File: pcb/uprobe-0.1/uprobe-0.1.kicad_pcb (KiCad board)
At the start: 2 copper layers, 33.5 x 77 mm, 5 parts, among them J1 uConsoleEXT

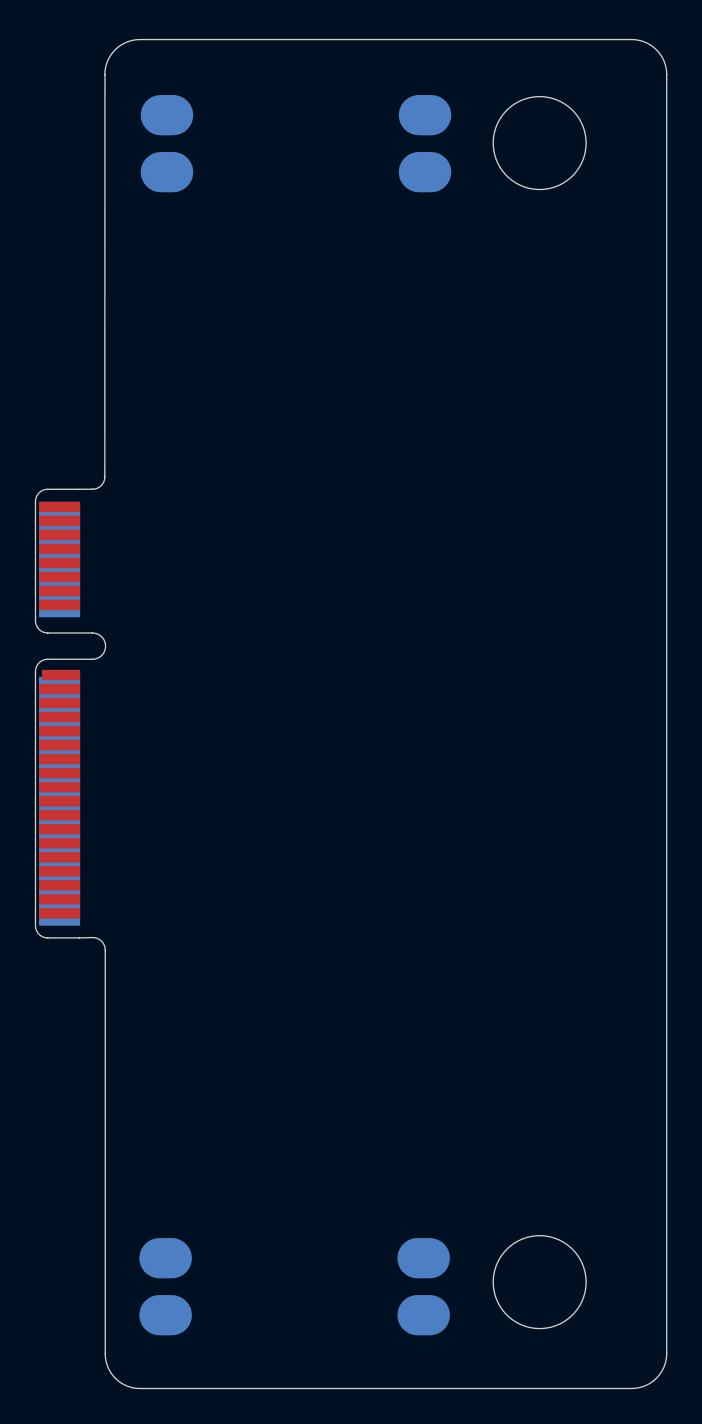
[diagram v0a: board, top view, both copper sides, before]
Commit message: working on usbasp section
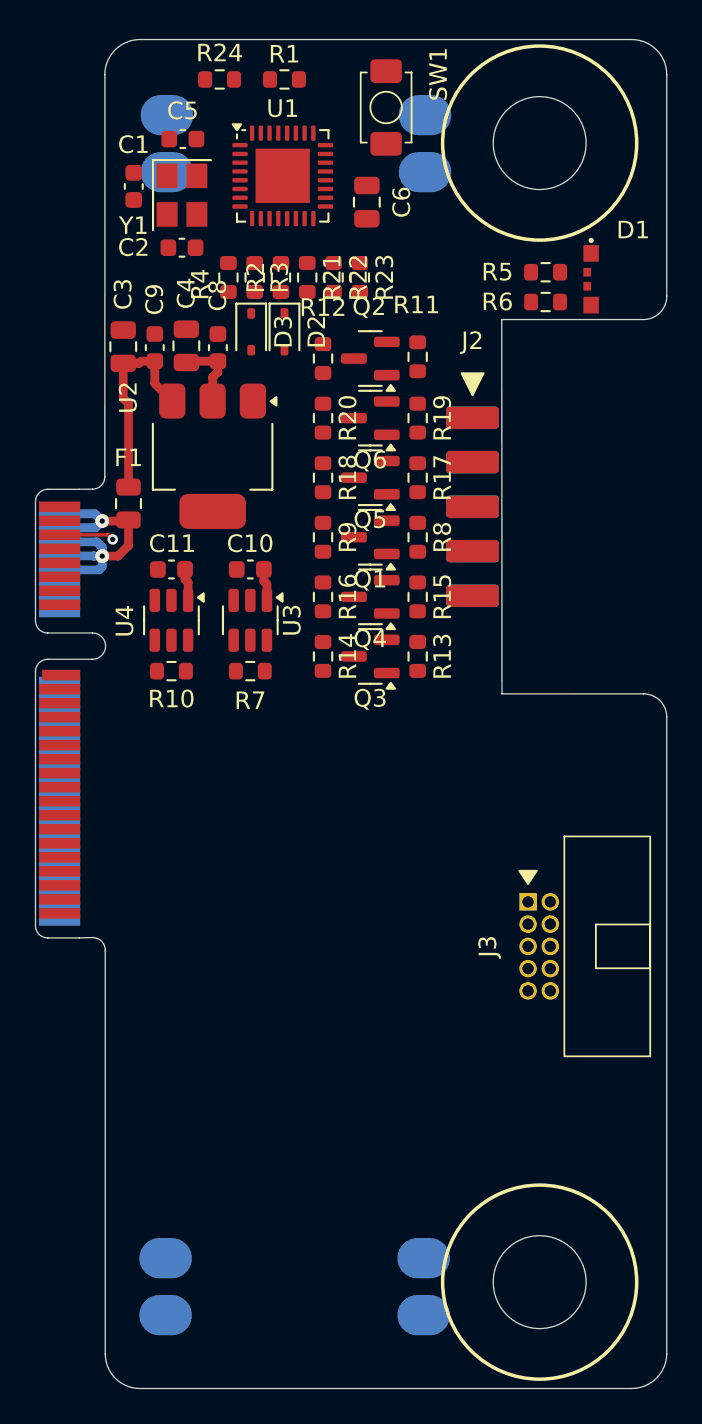
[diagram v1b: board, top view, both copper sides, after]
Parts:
- added C1: 27p, Capacitor_SMD:C_0603_1608Metric, F.Cu at (125.5, 70.9)
- added C10: 100n, Capacitor_SMD:C_0603_1608Metric, F.Cu at (132.2, 92.8)
- added C11: 100n, Capacitor_SMD:C_0603_1608Metric, F.Cu at (127.7, 92.8)
- added C2: 27p, Capacitor_SMD:C_0603_1608Metric, F.Cu at (128.2, 74.4)
- added C3: 10u, Capacitor_SMD:C_0805_2012Metric, F.Cu at (124.9, 80.0)
- added C4: 10u, Capacitor_SMD:C_0805_2012Metric, F.Cu at (128.5, 80.0)
- added C5: 100n, Capacitor_SMD:C_0603_1608Metric, F.Cu at (128.3, 68.2)
- added C6: 10u, Capacitor_SMD:C_0805_2012Metric, F.Cu at (138.8, 71.8)
- added C8: 100n, Capacitor_SMD:C_0603_1608Metric, F.Cu at (130.3, 80.1)
- added C9: 100n, Capacitor_SMD:C_0603_1608Metric, F.Cu at (126.7, 80.1)
- added D1: XL-3210SURUGC, uprobe:XL-3210SURUGC, F.Cu at (151.6, 76.2)
- added D2: 3V3, Diode_SMD:D_SOD-323, F.Cu at (134.1, 79.2)
- added D3: 3V3, Diode_SMD:D_SOD-323, F.Cu at (132.2, 79.2)
- added F1: 500mA, Fuse:Fuse_0805_2012Metric, F.Cu at (125.2, 89.0)
- added J2: Conn_02x05_Odd_Even, uprobe:IDC_2x05_SIDE, F.Cu at (144.8, 89.2)
- added J3: Conn_02x05_Odd_Even, uprobe:IDC_2x05_P1.27mm_Horizontal, F.Cu at (148.0, 114.3)
- added Q1: BSS138, Package_TO_SOT_SMD:SOT-23, F.Cu at (139.0, 90.9)
- added Q2: BSS138, Package_TO_SOT_SMD:SOT-23, F.Cu at (139.0, 80.7)
- added Q3: BSS138, Package_TO_SOT_SMD:SOT-23, F.Cu at (139.0, 97.7)
- added Q4: BSS138, Package_TO_SOT_SMD:SOT-23, F.Cu at (139.0, 94.3)
- added Q5: BSS138, Package_TO_SOT_SMD:SOT-23, F.Cu at (139.0, 87.5)
- added Q6: BSS138, Package_TO_SOT_SMD:SOT-23, F.Cu at (139.0, 84.1)
- added R1: 10k, Resistor_SMD:R_0603_1608Metric, F.Cu at (134.1, 64.8)
- added R10: 210k, Resistor_SMD:R_0603_1608Metric, F.Cu at (127.7, 98.6)
- added R11: 10k, Resistor_SMD:R_0603_1608Metric, F.Cu at (141.7, 80.6)
- added R12: 10k, Resistor_SMD:R_0603_1608Metric, F.Cu at (136.3, 80.7)
- added R13: 10k, Resistor_SMD:R_0603_1608Metric, F.Cu at (141.7, 97.7)
- added R14: 10k, Resistor_SMD:R_0603_1608Metric, F.Cu at (136.3, 97.7)
- added R15: 10k, Resistor_SMD:R_0603_1608Metric, F.Cu at (141.7, 94.3)
- added R16: 10k, Resistor_SMD:R_0603_1608Metric, F.Cu at (136.3, 94.3)
- added R17: 10k, Resistor_SMD:R_0603_1608Metric, F.Cu at (141.7, 87.5)
- added R18: 10k, Resistor_SMD:R_0603_1608Metric, F.Cu at (136.3, 87.5)
- added R19: 10k, Resistor_SMD:R_0603_1608Metric, F.Cu at (141.7, 84.1)
- added R2: 68, Resistor_SMD:R_0603_1608Metric, F.Cu at (133.9, 76.1)
- added R20: 10k, Resistor_SMD:R_0603_1608Metric, F.Cu at (136.3, 84.1)
- added R21: 270, Resistor_SMD:R_0603_1608Metric, F.Cu at (135.4, 76.1)
- added R22: 270, Resistor_SMD:R_0603_1608Metric, F.Cu at (136.9, 76.1)
- added R23: 270, Resistor_SMD:R_0603_1608Metric, F.Cu at (138.4, 76.1)
- added R24: 270, Resistor_SMD:R_0603_1608Metric, F.Cu at (130.4, 64.8)
- added R3: 68, Resistor_SMD:R_0603_1608Metric, F.Cu at (132.4, 76.1)
- added R4: 2k2, Resistor_SMD:R_0603_1608Metric, F.Cu at (130.9, 76.1)
- added R5: 1k, Resistor_SMD:R_0603_1608Metric, F.Cu at (149.0, 75.8)
- added R6: 1k, Resistor_SMD:R_0603_1608Metric, F.Cu at (149.0, 77.5)
- added R7: 210k, Resistor_SMD:R_0603_1608Metric, F.Cu at (132.2, 98.6)
- added R8: 10k, Resistor_SMD:R_0603_1608Metric, F.Cu at (141.7, 90.9)
- added R9: 10k, Resistor_SMD:R_0603_1608Metric, F.Cu at (136.3, 90.9)
- added SW1: XUNPU TS-1088-AR02016, uprobe:XUNPU_TS-1088-AR02016, F.Cu at (139.9, 66.4)
- added U1: ATmega8A-M, Package_DFN_QFN:QFN-32-1EP_5x5mm_P0.5mm_EP3.1x3.1mm, F.Cu at (134.0, 70.3)
- added U2: AMS1117-3.3, Package_TO_SOT_SMD:SOT-223-3_TabPin2, F.Cu at (130.0, 86.3)
- added U3: AP22653, Package_TO_SOT_SMD:SOT-23-6, F.Cu at (132.2, 95.7)
- added U4: AP22653, Package_TO_SOT_SMD:SOT-23-6, F.Cu at (127.7, 95.7)
- added Y1: ABM8-12.000MHZ-B2-T, Crystal:Crystal_SMD_Abracon_ABM8G-4Pin_3.2x2.5mm, F.Cu at (128.2, 71.4)
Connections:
- net +5V renamed VBUS
- J1 pad 13: unconnected-(J1-USB4_DP-Pad13) -> /USB4_D+
- J1 pad 15: unconnected-(J1-USB4_DM-Pad15) -> /USB4_D-
- J1 pad 18: unconnected-(J1-GPIO28-Pad18) -> /UASP_3V3_EN
- J1 pad 20: unconnected-(J1-GPIO29-Pad20) -> /UASP_5V_EN
- J1 pad 22: unconnected-(J1-GPIO30-Pad22) -> /~{UASP_3V3_FAULT}
- J1 pad 24: unconnected-(J1-GPIO31-Pad24) -> /~{UASP_5V_FAULT}
- J1 pad 26: unconnected-(J1-GPIO32-Pad26) -> /~{UASP_SLOW_SCK}
- J1 pad 7: unconnected-(J1-USB3_DP-Pad7) -> /USB3_D+
- J1 pad 9: unconnected-(J1-USB3_DM-Pad9) -> /USB3_D-
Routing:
- net VBUS: track 0.00 -> 18.6 mm, vias 0 -> 2
- net +5V: track 0.00 -> 13.6 mm
- net +3V3: track 0.00 -> 6.07 mm
- net GND: track 0.00 -> 3.14 mm, vias 0 -> 1
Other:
- outline, holes or cut-outs redrawn
- copper layers 2 -> 4

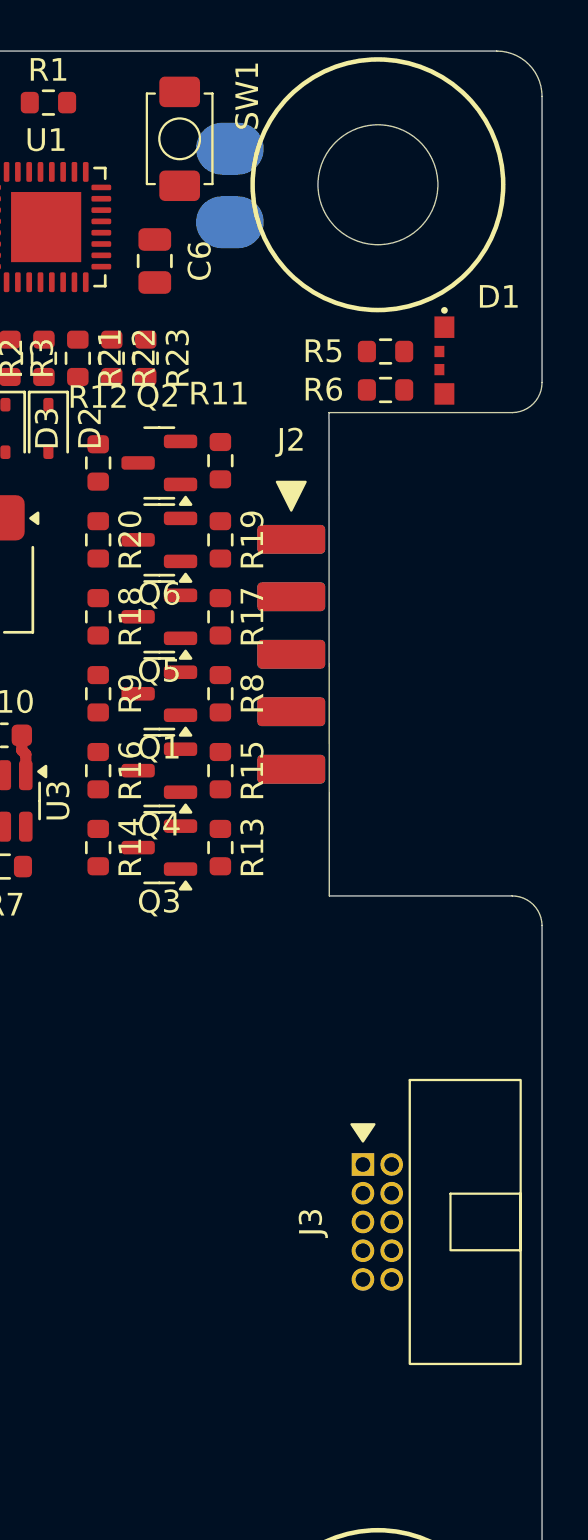
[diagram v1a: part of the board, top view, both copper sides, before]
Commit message: add level shifter sim, schema in prog
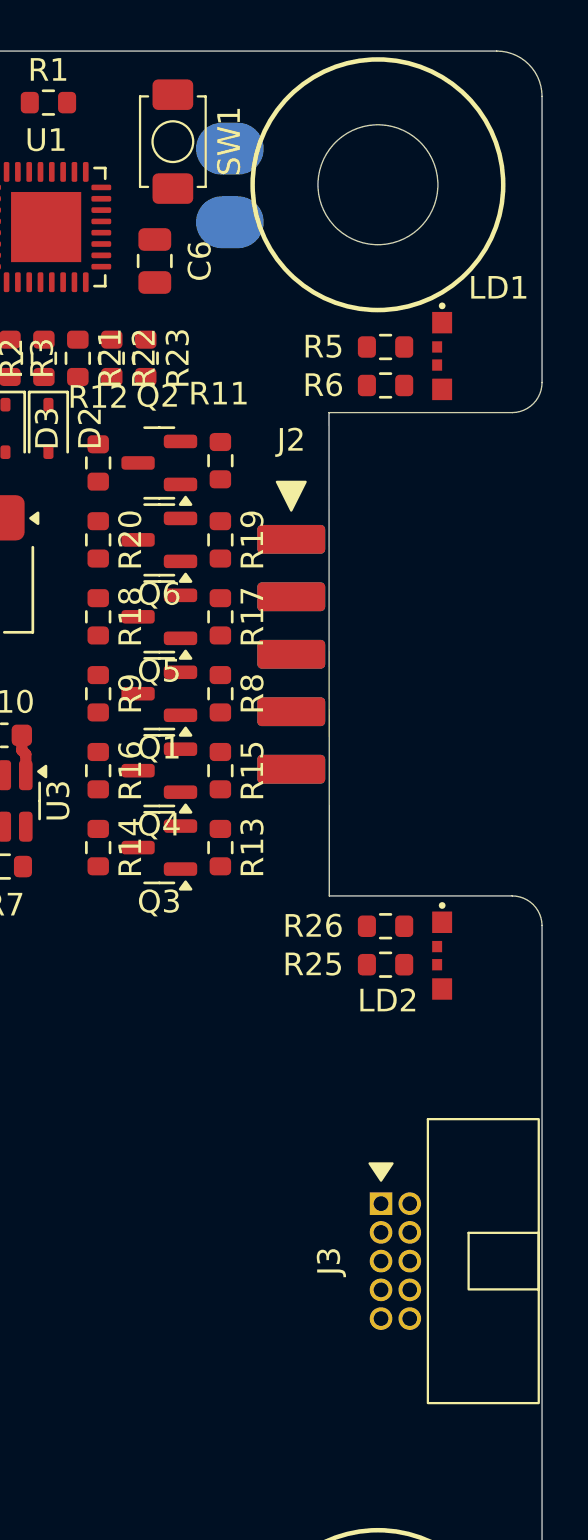
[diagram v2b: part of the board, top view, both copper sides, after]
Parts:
- removed D1: XL-3210SURUGC, uprobe:XL-3210SURUGC
- added LD1: XL-3210SURUGC, uprobe:XL-3210SURUGC, F.Cu at (151.5, 76.0)
- added LD2: XL-3210SURUGC, uprobe:XL-3210SURUGC, F.Cu at (151.5, 102.5)
- added R25: 1k, Resistor_SMD:R_0603_1608Metric, F.Cu at (149.0, 102.9)
- added R26: 270, Resistor_SMD:R_0603_1608Metric, F.Cu at (149.0, 101.2)
- moved J3 1.91 mm to (148.8, 116.0)
- moved SW1 0.33 mm to (139.6, 66.5)
- moved R5 0.20 mm to (149.0, 75.6)
- moved R6 0.20 mm to (149.0, 77.3)
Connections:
- J1 pad 22: /~{UASP_3V3_FAULT} -> /~{UASP_POWER_FAULT}
- J1 pad 24: /~{UASP_5V_FAULT} -> /~{UASP_SLOW_SCK}
- J1 pad 26: /~{UASP_SLOW_SCK} -> unconnected-(J1-GPIO32-Pad26)
- U3 pad 4: /~{UASP_5V_FAULT} -> /~{UASP_POWER_FAULT}
- U4 pad 4: /~{UASP_3V3_FAULT} -> /~{UASP_POWER_FAULT}

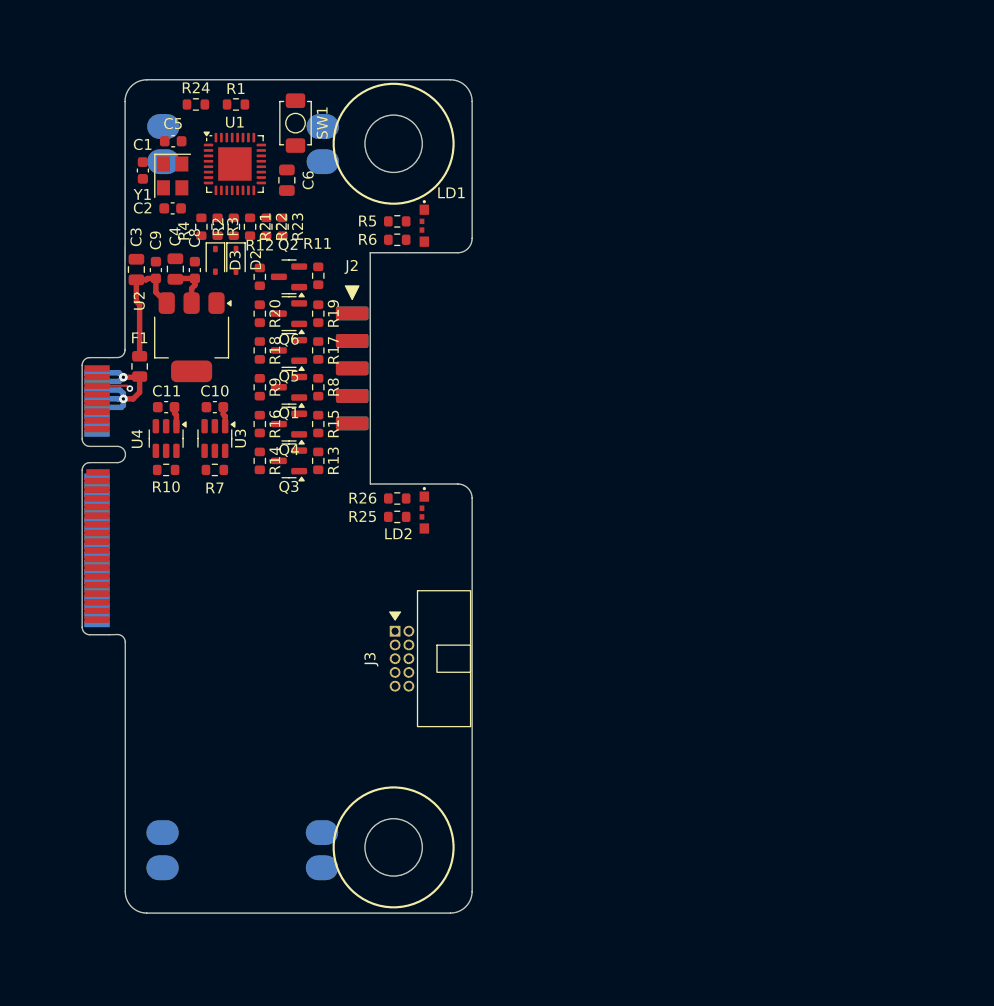
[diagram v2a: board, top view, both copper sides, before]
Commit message: add bmp schematics
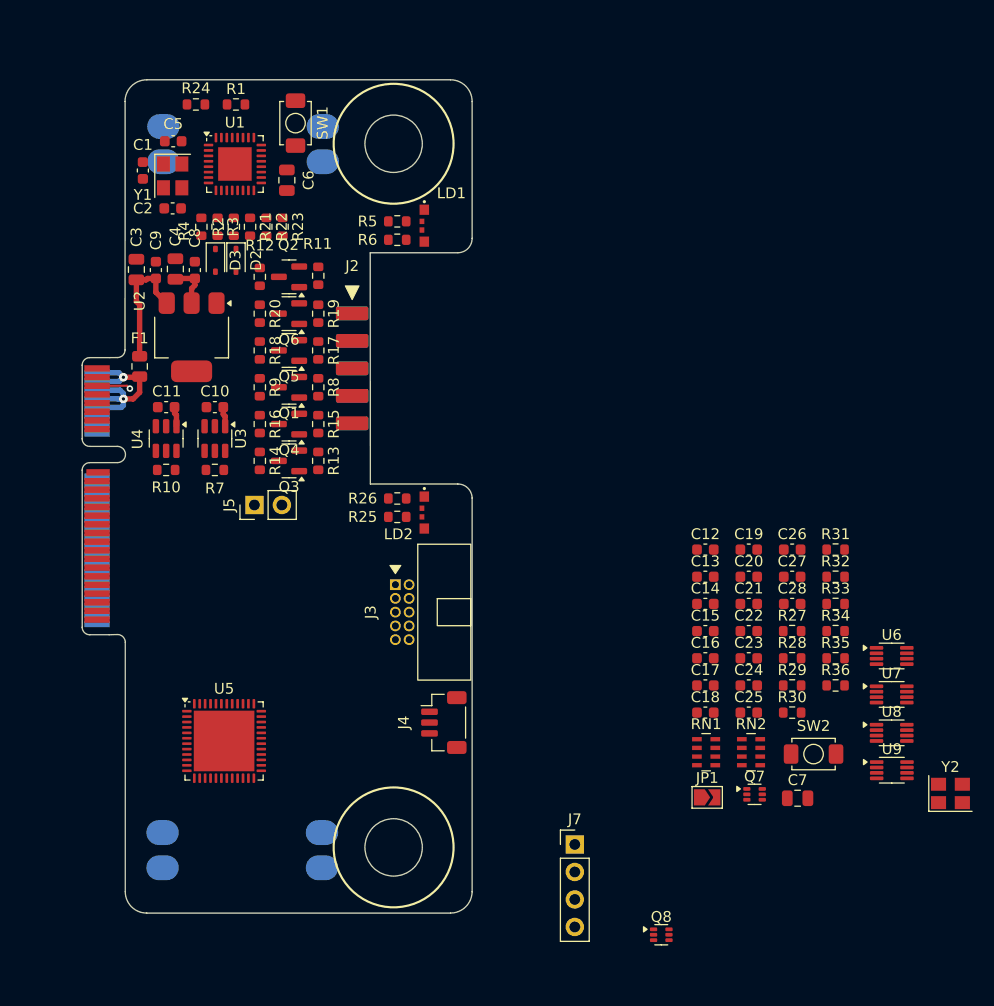
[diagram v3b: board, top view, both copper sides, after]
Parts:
- added C12: 100n, Capacitor_SMD:C_0603_1608Metric, F.Cu at (177.5, 105.9)
- added C13: 100n, Capacitor_SMD:C_0603_1608Metric, F.Cu at (177.5, 108.4)
- added C14: 100n, Capacitor_SMD:C_0603_1608Metric, F.Cu at (177.5, 110.9)
- added C15: 100n, Capacitor_SMD:C_0603_1608Metric, F.Cu at (177.5, 113.5)
- added C16: 100n, Capacitor_SMD:C_0603_1608Metric, F.Cu at (177.5, 116.0)
- added C17: 100n, Capacitor_SMD:C_0603_1608Metric, F.Cu at (177.5, 118.5)
- added C18: 100n, Capacitor_SMD:C_0603_1608Metric, F.Cu at (177.5, 121.0)
- added C19: 27p, Capacitor_SMD:C_0603_1608Metric, F.Cu at (181.5, 105.9)
- added C20: 27p, Capacitor_SMD:C_0603_1608Metric, F.Cu at (181.5, 108.4)
- added C21: 100n, Capacitor_SMD:C_0603_1608Metric, F.Cu at (181.5, 110.9)
- added C22: 100n, Capacitor_SMD:C_0603_1608Metric, F.Cu at (181.5, 113.5)
- added C23: 100n, Capacitor_SMD:C_0603_1608Metric, F.Cu at (181.5, 116.0)
- added C24: 100n, Capacitor_SMD:C_0603_1608Metric, F.Cu at (181.5, 118.5)
- added C25: 100n, Capacitor_SMD:C_0603_1608Metric, F.Cu at (181.5, 121.0)
- added C26: 100n, Capacitor_SMD:C_0603_1608Metric, F.Cu at (185.5, 105.9)
- added C27: 100n, Capacitor_SMD:C_0603_1608Metric, F.Cu at (185.5, 108.4)
- added C28: 100n, Capacitor_SMD:C_0603_1608Metric, F.Cu at (185.5, 110.9)
- added C7: 10u, Capacitor_SMD:C_0805_2012Metric, F.Cu at (186.0, 128.9)
- added J4: JST_SH_BM03B-SRSS, Connector_JST:JST_SH_BM03B-SRSS-TB_1x03-1MP_P1.00mm_Vertical, F.Cu at (153.3, 121.9)
- added J5: Conn_01x02, Connector_PinHeader_2.54mm:PinHeader_1x02_P2.54mm_Vertical, F.Cu at (135.8, 101.8)
- added J7: Conn_01x04, Connector_PinHeader_2.54mm:PinHeader_1x04_P2.54mm_Vertical, F.Cu at (165.4, 133.2)
- added JP1: SolderJumper_2_Open, Jumper:SolderJumper-2_P1.3mm_Open_TrianglePad1.0x1.5mm, F.Cu at (177.6, 128.8)
- added Q7: DMG1024UV, Package_TO_SOT_SMD:SOT-563, F.Cu at (182.0, 128.5)
- added Q8: DMG1023UV, Package_TO_SOT_SMD:SOT-563, F.Cu at (173.4, 141.5)
- added R27: 22, Resistor_SMD:R_0603_1608Metric, F.Cu at (185.5, 113.5)
- added R28: 22, Resistor_SMD:R_0603_1608Metric, F.Cu at (185.5, 116.0)
- added R29: 1k5, Resistor_SMD:R_0603_1608Metric, F.Cu at (185.5, 118.5)
- added R30: 4k7, Resistor_SMD:R_0603_1608Metric, F.Cu at (185.5, 121.0)
- added R31: 10k, Resistor_SMD:R_0603_1608Metric, F.Cu at (189.5, 105.9)
- added R32: 4k7, Resistor_SMD:R_0603_1608Metric, F.Cu at (189.5, 108.4)
- added R33: 4k7, Resistor_SMD:R_0603_1608Metric, F.Cu at (189.5, 110.9)
- added R34: 10k, Resistor_SMD:R_0603_1608Metric, F.Cu at (189.5, 113.5)
- added R35: 10k, Resistor_SMD:R_0603_1608Metric, F.Cu at (189.5, 116.0)
- added R36: 10k, Resistor_SMD:R_0603_1608Metric, F.Cu at (189.5, 118.5)
- added RN1: 100, Resistor_SMD:R_Array_Concave_4x0603, F.Cu at (177.5, 124.6)
- added RN2: 100, Resistor_SMD:R_Array_Concave_4x0603, F.Cu at (181.7, 124.6)
- added SW2: XUNPU TS-1088-AR02016, uprobe:XUNPU_TS-1088-AR02016, F.Cu at (187.5, 124.8)
- added U5: STM32F103CBUx, Package_DFN_QFN:QFN-48-1EP_7x7mm_P0.5mm_EP5.6x5.6mm, F.Cu at (133.0, 123.6)
- added U6: 74LVC2T45DC, Package_SO:VSSOP-8_2.3x2mm_P0.5mm, F.Cu at (194.7, 115.8)
- added U7: 74LVC2T45DC, Package_SO:VSSOP-8_2.3x2mm_P0.5mm, F.Cu at (194.7, 119.3)
- added U8: 74LVC2T45DC, Package_SO:VSSOP-8_2.3x2mm_P0.5mm, F.Cu at (194.7, 122.8)
- added U9: 74LVC2T45DC, Package_SO:VSSOP-8_2.3x2mm_P0.5mm, F.Cu at (194.7, 126.3)
- added Y2: ABM8-8.000MHZ-B2-T, Crystal:Crystal_SMD_Abracon_ABM8G-4Pin_3.2x2.5mm, F.Cu at (200.1, 128.4)
- moved J3 4.30 mm to (148.8, 111.7)
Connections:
- J3 pad 1: unconnected-(J3-Pin_1-Pad1) -> /TPWR
- J3 pad 10: unconnected-(J3-Pin_10-Pad10) -> /RST
- J3 pad 2: unconnected-(J3-Pin_2-Pad2) -> /TMS
- J3 pad 3: unconnected-(J3-Pin_3-Pad3) -> GND
- J3 pad 4: unconnected-(J3-Pin_4-Pad4) -> /TCK
- J3 pad 5: unconnected-(J3-Pin_5-Pad5) -> GND
- J3 pad 6: unconnected-(J3-Pin_6-Pad6) -> /TDO
- J3 pad 8: unconnected-(J3-Pin_8-Pad8) -> /TDI
- J3 pad 9: unconnected-(J3-Pin_9-Pad9) -> GND
